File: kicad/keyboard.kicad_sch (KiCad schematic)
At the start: 64 parts

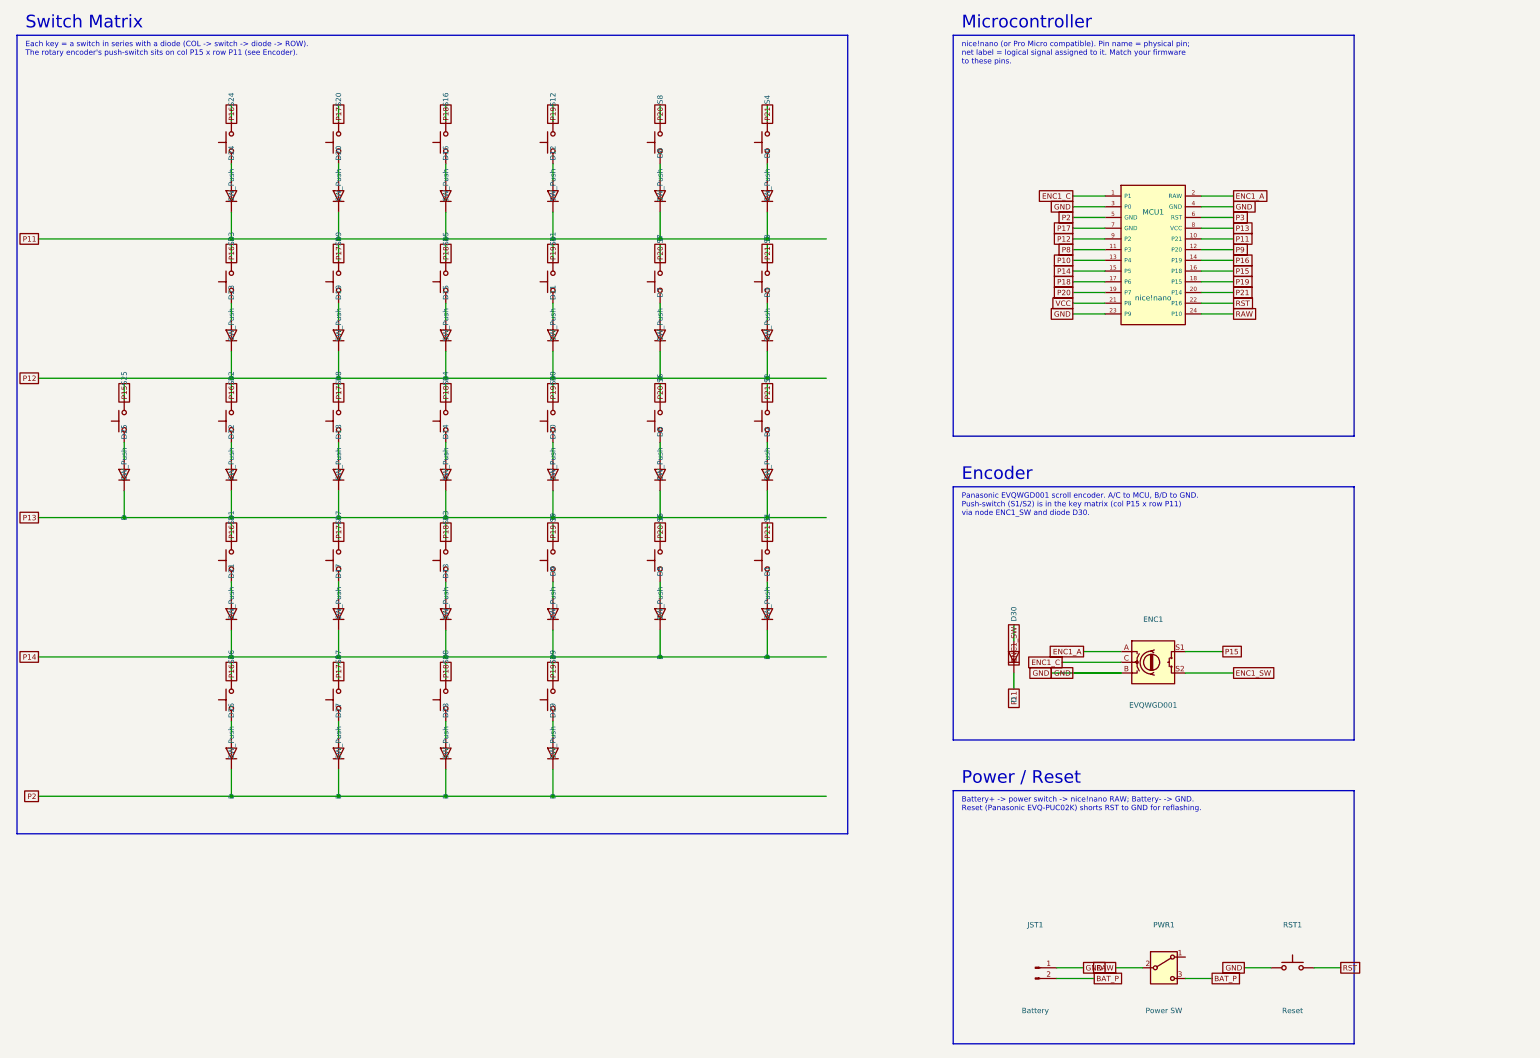
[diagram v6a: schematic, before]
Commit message: Cleaner matrix: single-label COL/ROW bus rails, hide clutter
Rework the switch matrix to read like the reference schematic:
- Full vertical COL rails and horizontal ROW rails that cross freely (KiCad
  keeps crossing wires separate); each switch/diode taps its rail with a
  junction. COL/ROW names are now labelled ONCE per rail instead of on every
  cell, eliminating the overlapping-label clutter.
- Hide the redundant SW_Push/D value text and shrink + offset the reference
  designators so they don't overlap wires or neighbours.
- Wider column spacing (30.48mm) for legibility.
Connectivity verified unchanged (54 nets; columns=switches+MCU, rows=diodes+
MCU, encoder/power all correct).
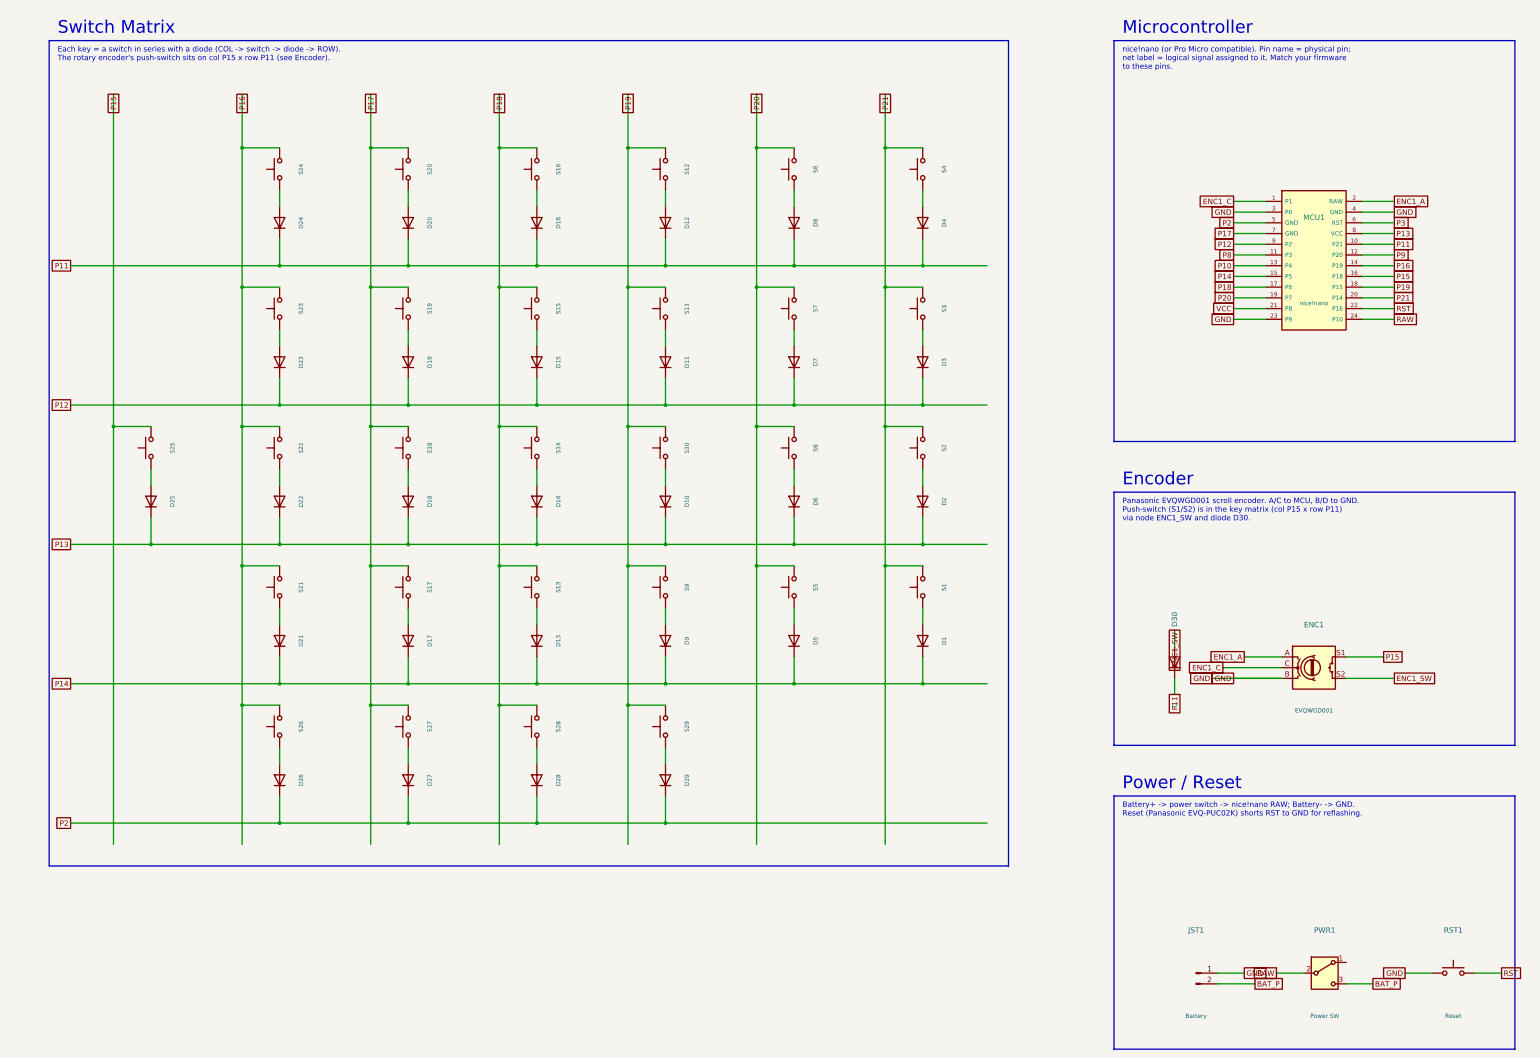
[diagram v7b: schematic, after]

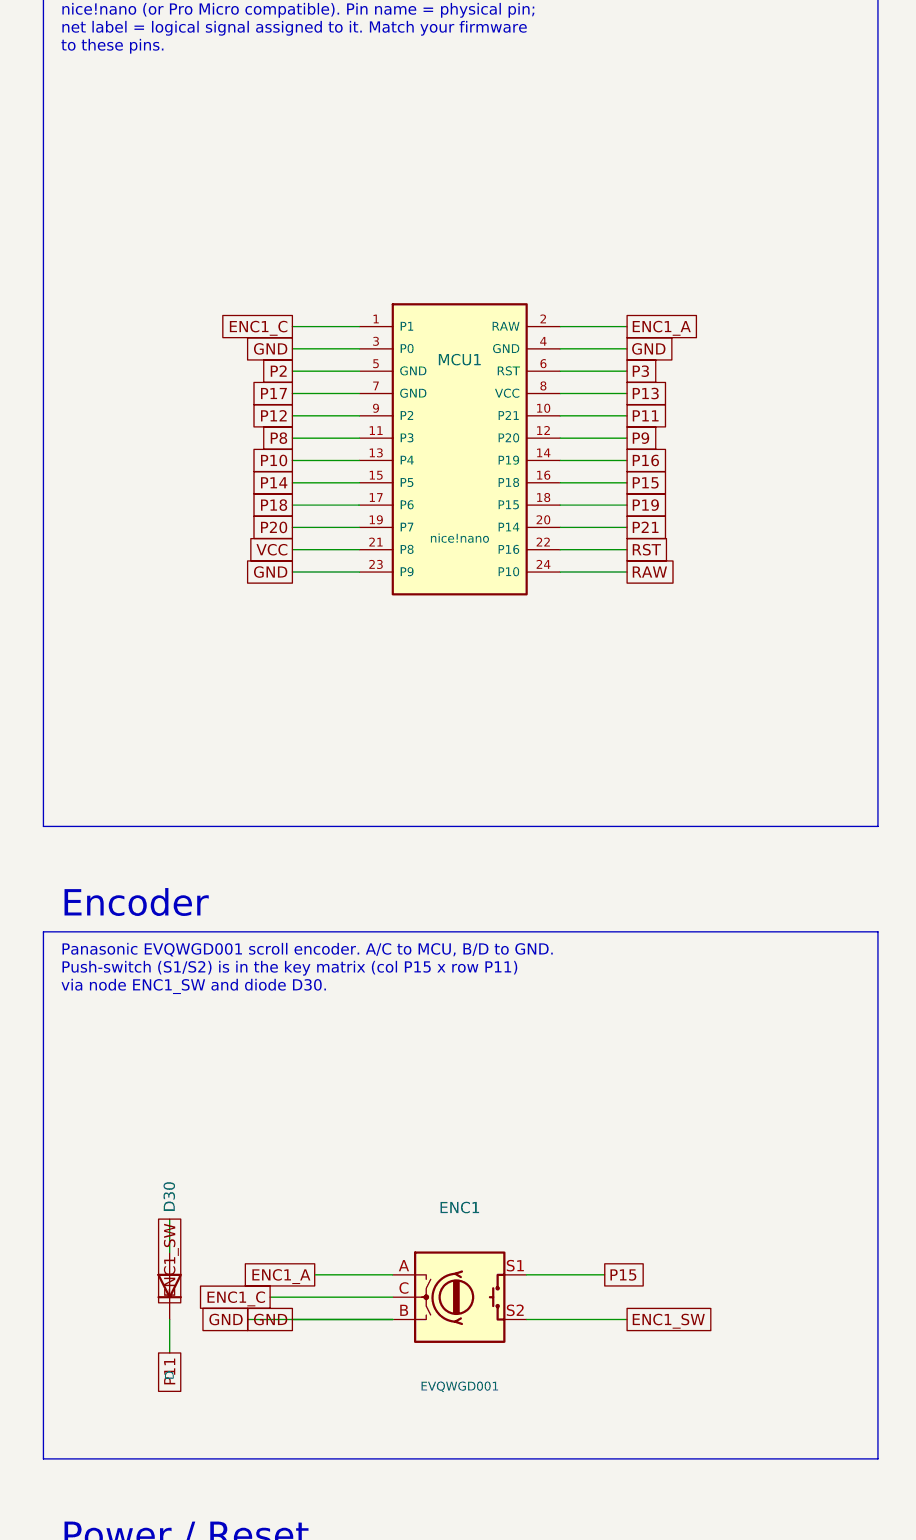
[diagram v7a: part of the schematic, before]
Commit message: Fix overlapping text/labels: roomier nice!nano pitch + tidy refs
Full readability pass:
- nice!nano symbol pins now on 5.08mm pitch (was 2.54) with a wider body, so
  the physical pin names and net labels no longer overlap (removed 22 of 23
  close-label collisions in the MCU block).
- Encoder push-switch diode (D30) reference offset to the side + value hidden
  so it no longer collides with the ENC1_SW label (last remaining overlap).
- Verified: 0 text/label pairs closer than 3mm; no reference designators on
  wires; connectivity unchanged (54 nets).
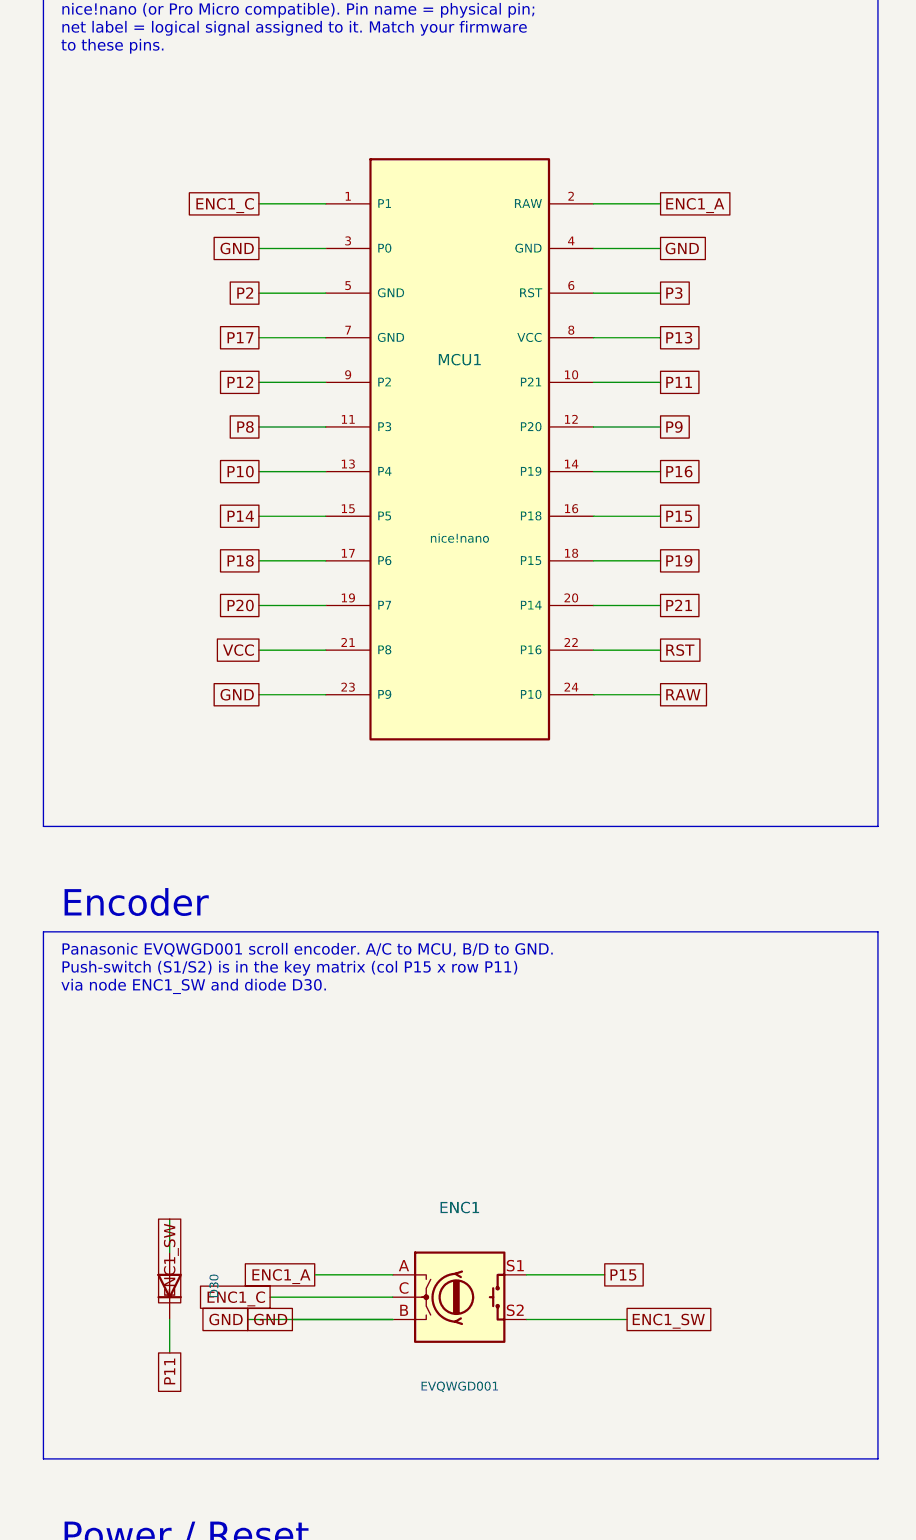
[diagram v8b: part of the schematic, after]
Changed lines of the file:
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@@
       (effects (font (size 1.0 1.0))))
   )
-  (wire (pts (xy 363.22 97.79) (xy 370.84 97.79)) (stroke (width 0) (type default)))
-  (global_label "RAW" (shape passive) (at 370.84 97.79 0)
+  (wire (pts (xy 367.03 111.76) (xy 374.65 111.76)) (stroke (width 0) (type default)))
+  (global_label "RAW" (shape passive) (at 374.65 111.76 0)
     (effects (font (size 1.27 1.27)) (justify left)))
-  (wire (pts (xy 340.36 69.85) (xy 332.74 69.85)) (stroke (width 0) (type default)))
-  (global_label "ENC1_C" (shape passive) (at 332.74 69.85 0)
+  (wire (pts (xy 336.55 55.88) (xy 328.93 55.88)) (stroke (width 0) (type default)))
+  (global_label "ENC1_C" (shape passive) (at 328.93 55.88 0)
     (effects (font (size 1.27 1.27)) (justify right)))
-  (wire (pts (xy 340.36 97.79) (xy 332.74 97.79)) (stroke (width 0) (type default)))
-  (global_label "GND" (shape passive) (at 332.74 97.79 0)
+  (wire (pts (xy 336.55 111.76) (xy 328.93 111.76)) (stroke (width 0) (type default)))
+  (global_label "GND" (shape passive) (at 328.93 111.76 0)
     (effects (font (size 1.27 1.27)) (justify right)))
-  (wire (pts (xy 363.22 69.85) (xy 370.84 69.85)) (stroke (width 0) (type default)))
-  (global_label "ENC1_A" (shape passive) (at 370.84 69.85 0)
+  (wire (pts (xy 367.03 55.88) (xy 374.65 55.88)) (stroke (width 0) (type default)))
+  (global_label "ENC1_A" (shape passive) (at 374.65 55.88 0)
     (effects (font (size 1.27 1.27)) (justify left)))
-  (wire (pts (xy 363.22 95.25) (xy 370.84 95.25)) (stroke (width 0) (type default)))
-  (global_label "RST" (shape passive) (at 370.84 95.25 0)
+  (wire (pts (xy 367.03 106.68) (xy 374.65 106.68)) (stroke (width 0) (type default)))
+  (global_label "RST" (shape passive) (at 374.65 106.68 0)
     (effects (font (size 1.27 1.27)) (justify left)))
-  (wire (pts (xy 340.36 72.39) (xy 332.74 72.39)) (stroke (width 0) (type default)))
-  (global_label "GND" (shape passive) (at 332.74 72.39 0)
+  (wire (pts (xy 336.55 60.96) (xy 328.93 60.96)) (stroke (width 0) (type default)))
+  (global_label "GND" (shape passive) (at 328.93 60.96 0)
     (effects (font (size 1.27 1.27)) (justify right)))
-  (wire (pts (xy 340.36 95.25) (xy 332.74 95.25)) (stroke (width 0) (type default)))
-  (global_label "VCC" (shape passive) (at 332.74 95.25 0)
+  (wire (pts (xy 336.55 106.68) (xy 328.93 106.68)) (stroke (width 0) (type default)))
+  (global_label "VCC" (shape passive) (at 328.93 106.68 0)
     (effects (font (size 1.27 1.27)) (justify right)))
-  (wire (pts (xy 363.22 72.39) (xy 370.84 72.39)) (stroke (width 0) (type default)))
-  (global_label "GND" (shape passive) (at 370.84 72.39 0)
+  (wire (pts (xy 367.03 60.96) (xy 374.65 60.96)) (stroke (width 0) (type default)))
+  (global_label "GND" (shape passive) (at 374.65 60.96 0)
     (effects (font (size 1.27 1.27)) (justify left)))
-  (wire (pts (xy 363.22 92.71) (xy 370.84 92.71)) (stroke (width 0) (type default)))
-  (global_label "P21" (shape passive) (at 370.84 92.71 0)
+  (wire (pts (xy 367.03 101.60) (xy 374.65 101.60)) (stroke (width 0) (type default)))
+  (global_label "P21" (shape passive) (at 374.65 101.60 0)
     (effects (font (size 1.27 1.27)) (justify left)))
-  (wire (pts (xy 340.36 74.93) (xy 332.74 74.93)) (stroke (width 0) (type default)))
-  (global_label "P2" (shape passive) (at 332.74 74.93 0)
+  (wire (pts (xy 336.55 66.04) (xy 328.93 66.04)) (stroke (width 0) (type default)))
+  (global_label "P2" (shape passive) (at 328.93 66.04 0)
     (effects (font (size 1.27 1.27)) (justify right)))
-  (wire (pts (xy 340.36 92.71) (xy 332.74 92.71)) (stroke (width 0) (type default)))
-  (global_label "P20" (shape passive) (at 332.74 92.71 0)
+  (wire (pts (xy 336.55 101.60) (xy 328.93 101.60)) (stroke (width 0) (type default)))
+  (global_label "P20" (shape passive) (at 328.93 101.60 0)
     (effects (font (size 1.27 1.27)) (justify right)))
-  (wire (pts (xy 363.22 74.93) (xy 370.84 74.93)) (stroke (width 0) (type default)))
-  (global_label "P3" (shape passive) (at 370.84 74.93 0)
+  (wire (pts (xy 367.03 66.04) (xy 374.65 66.04)) (stroke (width 0) (type default)))
+  (global_label "P3" (shape passive) (at 374.65 66.04 0)
     (effects (font (size 1.27 1.27)) (justify left)))
-  (wire (pts (xy 363.22 90.17) (xy 370.84 90.17)) (stroke (width 0) (type default)))
-  (global_label "P19" (shape passive) (at 370.84 90.17 0)
+  (wire (pts (xy 367.03 96.52) (xy 374.65 96.52)) (stroke (width 0) (type default)))
+  (global_label "P19" (shape passive) (at 374.65 96.52 0)
     (effects (font (size 1.27 1.27)) (justify left)))
-  (wire (pts (xy 340.36 77.47) (xy 332.74 77.47)) (stroke (width 0) (type default)))
-  (global_label "P17" (shape passive) (at 332.74 77.47 0)
+  (wire (pts (xy 336.55 71.12) (xy 328.93 71.12)) (stroke (width 0) (type default)))
+  (global_label "P17" (shape passive) (at 328.93 71.12 0)
     (effects (font (size 1.27 1.27)) (justify right)))
-  (wire (pts (xy 340.36 90.17) (xy 332.74 90.17)) (stroke (width 0) (type default)))
-  (global_label "P18" (shape passive) (at 332.74 90.17 0)
+  (wire (pts (xy 336.55 96.52) (xy 328.93 96.52)) (stroke (width 0) (type default)))
+  (global_label "P18" (shape passive) (at 328.93 96.52 0)
     (effects (font (size 1.27 1.27)) (justify right)))
-  (wire (pts (xy 363.22 77.47) (xy 370.84 77.47)) (stroke (width 0) (type default)))
-  (global_label "P13" (shape passive) (at 370.84 77.47 0)
+  (wire (pts (xy 367.03 71.12) (xy 374.65 71.12)) (stroke (width 0) (type default)))
+  (global_label "P13" (shape passive) (at 374.65 71.12 0)
     (effects (font (size 1.27 1.27)) (justify left)))
-  (wire (pts (xy 363.22 87.63) (xy 370.84 87.63)) (stroke (width 0) (type default)))
-  (global_label "P15" (shape passive) (at 370.84 87.63 0)
+  (wire (pts (xy 367.03 91.44) (xy 374.65 91.44)) (stroke (width 0) (type default)))
+  (global_label "P15" (shape passive) (at 374.65 91.44 0)
     (effects (font (size 1.27 1.27)) (justify left)))
-  (wire (pts (xy 340.36 80.01) (xy 332.74 80.01)) (stroke (width 0) (type default)))
-  (global_label "P12" (shape passive) (at 332.74 80.01 0)
+  (wire (pts (xy 336.55 76.20) (xy 328.93 76.20)) (stroke (width 0) (type default)))
+  (global_label "P12" (shape passive) (at 328.93 76.20 0)
     (effects (font (size 1.27 1.27)) (justify right)))
-  (wire (pts (xy 340.36 87.63) (xy 332.74 87.63)) (stroke (width 0) (type default)))
-  (global_label "P14" (shape passive) (at 332.74 87.63 0)
+  (wire (pts (xy 336.55 91.44) (xy 328.93 91.44)) (stroke (width 0) (type default)))
+  (global_label "P14" (shape passive) (at 328.93 91.44 0)
     (effects (font (size 1.27 1.27)) (justify right)))
-  (wire (pts (xy 363.22 80.01) (xy 370.84 80.01)) (stroke (width 0) (type default)))
-  (global_label "P11" (shape passive) (at 370.84 80.01 0)
+  (wire (pts (xy 367.03 76.20) (xy 374.65 76.20)) (stroke (width 0) (type default)))
+  (global_label "P11" (shape passive) (at 374.65 76.20 0)
     (effects (font (size 1.27 1.27)) (justify left)))
-  (wire (pts (xy 363.22 85.09) (xy 370.84 85.09)) (stroke (width 0) (type default)))
-  (global_label "P16" (shape passive) (at 370.84 85.09 0)
+  (wire (pts (xy 367.03 86.36) (xy 374.65 86.36)) (stroke (width 0) (type default)))
+  (global_label "P16" (shape passive) (at 374.65 86.36 0)
     (effects (font (size 1.27 1.27)) (justify left)))
-  (wire (pts (xy 340.36 82.55) (xy 332.74 82.55)) (stroke (width 0) (type default)))
-  (global_label "P8" (shape passive) (at 332.74 82.55 0)
+  (wire (pts (xy 336.55 81.28) (xy 328.93 81.28)) (stroke (width 0) (type default)))
+  (global_label "P8" (shape passive) (at 328.93 81.28 0)
     (effects (font (size 1.27 1.27)) (justify right)))
-  (wire (pts (xy 340.36 85.09) (xy 332.74 85.09)) (stroke (width 0) (type default)))
-  (global_label "P10" (shape passive) (at 332.74 85.09 0)
+  (wire (pts (xy 336.55 86.36) (xy 328.93 86.36)) (stroke (width 0) (type default)))
+  (global_label "P10" (shape passive) (at 328.93 86.36 0)
     (effects (font (size 1.27 1.27)) (justify right)))
-  (wire (pts (xy 363.22 82.55) (xy 370.84 82.55)) (stroke (width 0) (type default)))
-  (global_label "P9" (shape passive) (at 370.84 82.55 0)
+  (wire (pts (xy 367.03 81.28) (xy 374.65 81.28)) (stroke (width 0) (type default)))
+  (global_label "P9" (shape passive) (at 374.65 81.28 0)
     (effects (font (size 1.27 1.27)) (justify left)))
   (rectangle (start 304.40 138.75) (end 399.40 198.75)
@@
   (symbol (lib_id "Device:D") (at 318.77 179.07 90) (unit 1)
     (in_bom yes) (on_board yes) (dnp no)
-    (property "Reference" "D30" (at 318.77 168.91 0)
-      (effects (font (size 1.27 1.27))))
+    (property "Reference" "D30" (at 323.85 179.07 0)
+      (effects (font (size 1.0 1.0))))
     (property "Value" "D" (at 318.77 189.23 0)
-      (effects (font (size 1.0 1.0))))
+      (effects (font (size 1.0 1.0))) (hide yes))
   )
   (wire (pts (xy 318.77 175.26) (xy 318.77 171.45)) (stroke (width 0) (type default)))
